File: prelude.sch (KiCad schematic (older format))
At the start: 34 parts, among them J1 CONN_01X50, J2 USB_C, J3 CONN_01X04, SW1 SW_Push, U1 LM3671MF-3.3, U2 STM32F103RETx, U3 AP5724, Y1 16MHz

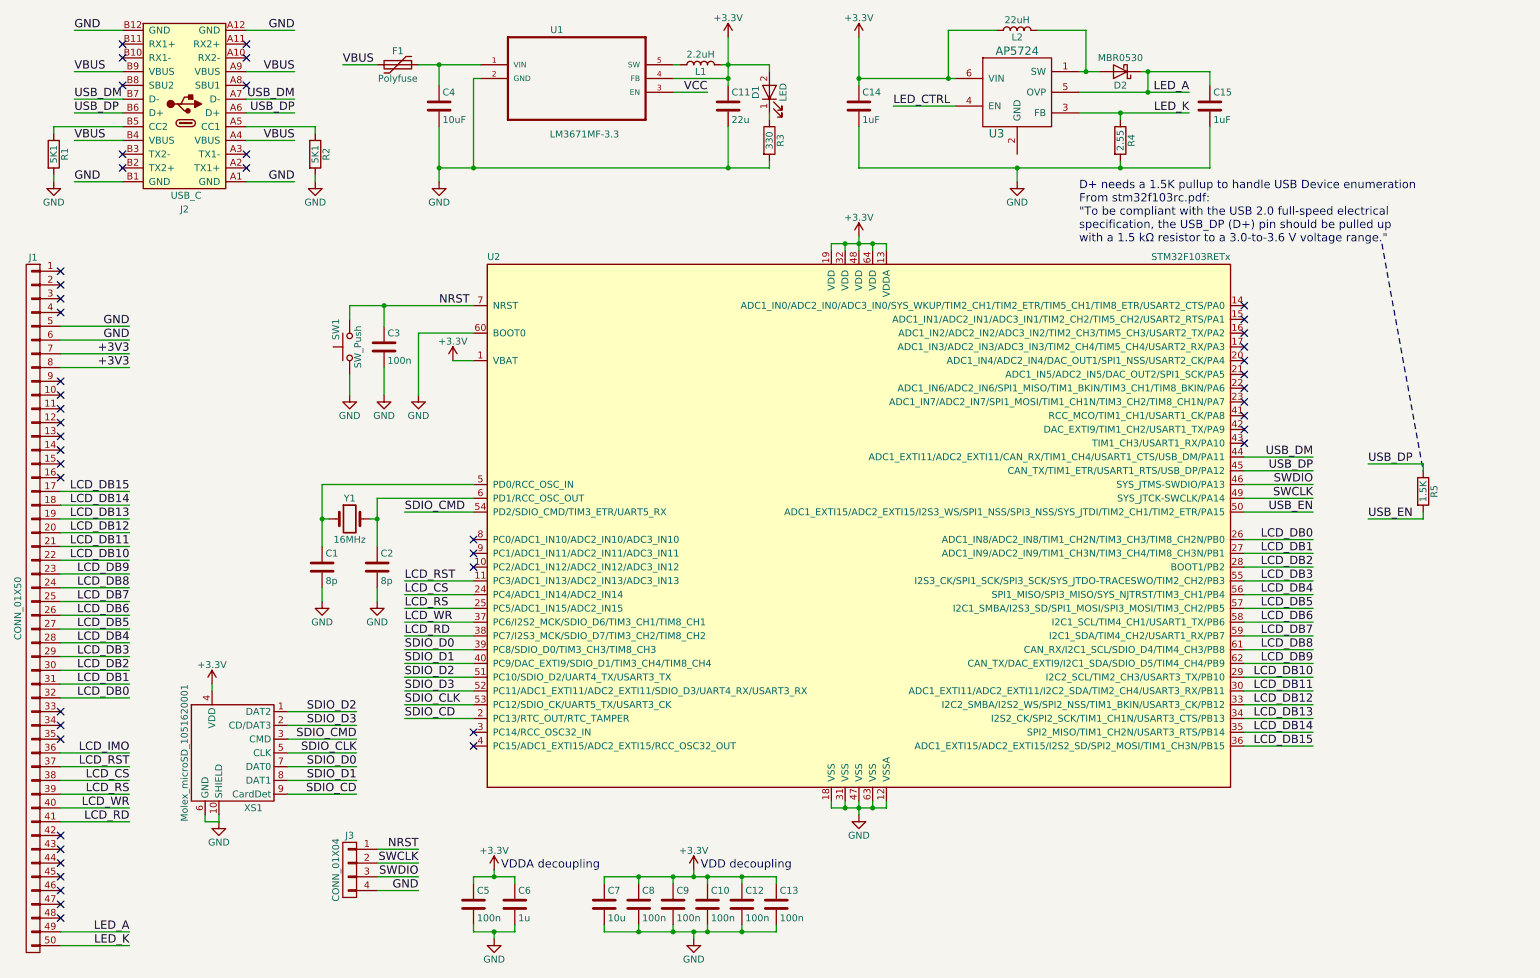
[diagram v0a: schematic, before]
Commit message: Moved to STM32F411RE
Had to move to different MCU (STM32F411RE) because I2C bus was fixed to pins on B bus, which was used for LCD data bus, and SDIO was also fixed to C bus.
Remapped LCD data bus to C bus since it allows having all other functionality (SDIO, I2C, USB) correctly mapped.
Redid CvPcb and net generation.
Started PCB routing with MCU pins 49-64 facing LCD connector.
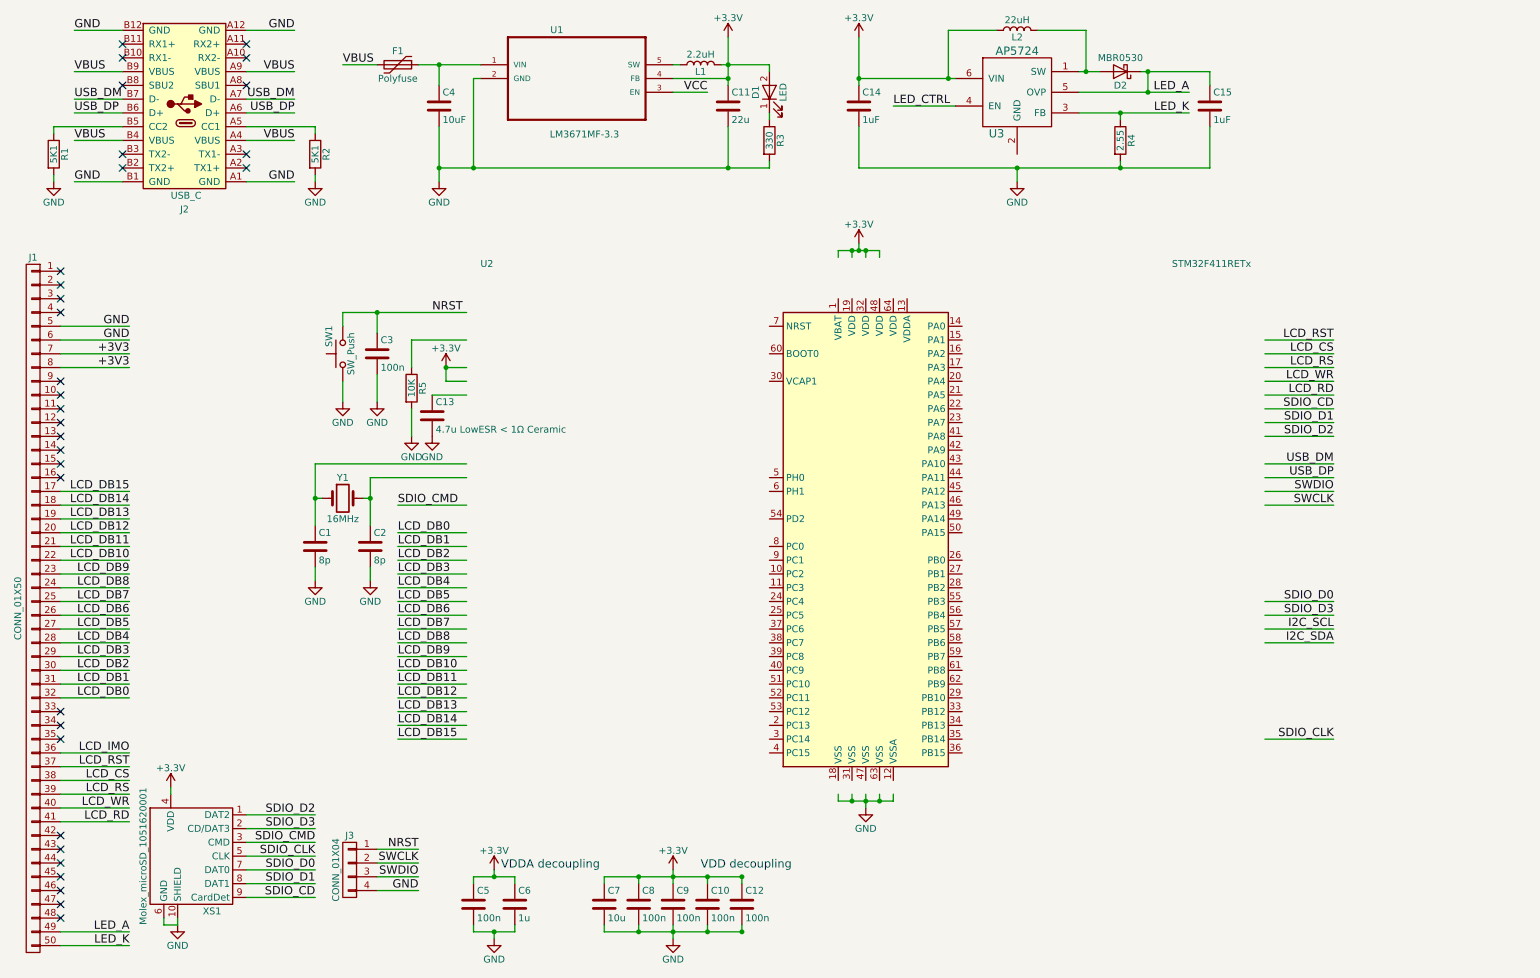
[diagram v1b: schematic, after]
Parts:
- removed U2: STM32F103RETx, Housings_QFP:LQFP-64_10x10mm_Pitch0.5mm, symbol STM32F103RETx
- added U2: STM32F411RETx, LQFP64, symbol STM32F411RETx
- C13: value 100n -> 4.7u LowESR < 1Ω Ceramic
- R5: value 1.5K -> 10K; footprint Resistors_SMD:R_0805 -> (none)
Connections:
- net labels added: I2C_SCL, I2C_SDA
- net labels removed: USB_EN
- wire segments 185 -> 217
- no-connect marks 48 -> 32
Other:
- note removed: "D+ needs a 1.5K pullup to handle USB Device enumeration\nFrom stm32f103rc.pdf:\n"To be compliant with the USB 2.0 full-speed electrical\nspecification, the USB_DP (D+) pin should be pulled up\nwith a 1.5 kΩ resistor to a 3.0-to-3.6 V voltage range.""
- moved on the sheet: C1, C2, C3, SW1, XS1, Y1

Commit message: A lot of changes, just need to add more polish and clean up
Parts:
- removed XS1: Molex_microSD_1051620001, volium:Molex_1051620001, symbol Molex_microSD_1051620001
- added J4: CONN_01X08, volium:WE_68710814022, symbol CONN_01X08
- added R6: 10K, Resistors_SMD:R_0805, symbol R
- added XS1: SD_ebay-uSD-push/push_SMD, volium:Conn_uSDcard, symbol SD_ebay-uSD-push/push_SMD
- J2: footprint volium:DX07S024XJ1 -> volium:Amphenol_12401548E4#2A
- J3: footprint Pin_Headers:Pin_Header_Angled_1x04_Pitch2.54mm -> volium:M20-8890445
- R5: footprint (none) -> Resistors_SMD:R_0805
- U2: footprint LQFP64 -> Housings_QFP:LQFP-64_10x10mm_Pitch0.5mm
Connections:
- net labels added: TS_INT, TS_RST, TS_SCL, TS_SDA, USB_D+, USB_D-
- net labels removed: I2C_SCL, I2C_SDA
- wire segments 217 -> 192
- no-connect marks 32 -> 33
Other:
- note added: "Pin 32"
- note added: "Pin 48"
- note added: "Pin 64"

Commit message: Updates project after loading with KiCad 5.0.2
Replaced schematic symbols and pcb footprints with new versions
Regenerated netlist after all changes
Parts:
- removed J3: CONN_01X04, volium:M20-8890445, symbol CONN_01X04
- removed J4: CONN_01X08, volium:WE_68710814022, symbol CONN_01X08
- removed SW1: SW_Push, Buttons_Switches_SMD:SW_SPST_PTS645, symbol SW_Push
- removed U2: STM32F411RETx, Housings_QFP:LQFP-64_10x10mm_Pitch0.5mm, symbol STM32F411RETx
- removed XS1: SD_ebay-uSD-push/push_SMD, volium:Conn_uSDcard, symbol SD_ebay-uSD-push/push_SMD
- added J3: Conn_01x04, volium:M20-8890445, symbol Connector_Generic:Conn_01x04
- added J4: Conn_01x08, volium:WE_68710814022, symbol Connector_Generic:Conn_01x08
- added SW1: SW_Push, Button_Switch_SMD:SW_SPST_PTS645, symbol Switch:SW_Push
- added U2: STM32F411RETx, Package_QFP:LQFP-64_10x10mm_P0.5mm, symbol MCU_ST_STM32F4:STM32F411RETx
- added XS1: SD_ebay-uSD-push_push_SMD, volium:Conn_uSDcard, symbol volium:SD_ebay-uSD-push_push_SMD
- C1, C10, C11, C12, C13, C14, C15, C2, C3, C4, C5, C6, C7, C8, C9: footprint Capacitors_SMD:C_0805 -> Capacitor_SMD:C_0805_2012Metric_Pad1.15x1.40mm_HandSolder; symbol C -> Device:C
- D1: footprint LEDs:LED_0805 -> LED_SMD:LED_0805_2012Metric_Pad1.15x1.40mm_HandSolder; symbol LED -> Device:LED
- D2: footprint Diodes_SMD:D_SOD-123 -> Diode_SMD:D_SOD-123; symbol D_Schottky -> Device:D_Schottky
- F1: symbol Polyfuse -> Device:Polyfuse
- J1: symbol CONN_01X50 -> volium:CONN_01X50
- J2: symbol USB_C -> volium:USB_C
- L1: footprint Inductors:Inductor_Taiyo-Yuden_NR-24xx -> Inductor_SMD:L_Taiyo-Yuden_NR-24xx_HandSoldering; symbol L -> Device:L
- L2: footprint Inductors:Inductor_Taiyo-Yuden_NR-30xx -> Inductor_SMD:L_Taiyo-Yuden_NR-30xx_HandSoldering; symbol L -> Device:L
- R1, R2, R3, R4, R5, R6: footprint Resistors_SMD:R_0805 -> Resistor_SMD:R_0805_2012Metric_Pad1.15x1.40mm_HandSolder; symbol R -> Device:R
- U1: footprint TO_SOT_Packages_SMD:TSOT-23-5 -> Package_TO_SOT_SMD:SOT-23-5_HandSoldering; symbol LM3671MF-3.3 -> volium:LM3671MF-3.3
- U3: footprint TO_SOT_Packages_SMD:SOT-23-6 -> Package_TO_SOT_SMD:SOT-23-6_Handsoldering; symbol AP5724 -> volium:AP5724
- Y1: footprint Crystals:Crystal_SMD_5032-2pin_5.0x3.2mm -> Crystal:Crystal_SMD_5032-2Pin_5.0x3.2mm_HandSoldering; symbol Crystal -> Device:Crystal
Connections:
- net labels removed: LCD_IMO, USB_DM, USB_DP
- wire segments 192 -> 231
- no-connect marks 33 -> 45
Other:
- moved on the sheet: C1, C13, C2, C3, R5, Y1

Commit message: Replaces passive components with regular (non-HandSolder) versions
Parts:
- C1, C10, C11, C12, C13, C14, C15, C2, C3, C4, C5, C6, C7, C8, C9: footprint Capacitor_SMD:C_0805_2012Metric_Pad1.15x1.40mm_HandSolder -> Capacitor_SMD:C_0805_2012Metric
- D1: footprint LED_SMD:LED_0805_2012Metric_Pad1.15x1.40mm_HandSolder -> LED_SMD:LED_0805_2012Metric
- L1: footprint Inductor_SMD:L_Taiyo-Yuden_NR-24xx_HandSoldering -> Inductor_SMD:L_Taiyo-Yuden_NR-24xx
- L2: footprint Inductor_SMD:L_Taiyo-Yuden_NR-30xx_HandSoldering -> Inductor_SMD:L_Taiyo-Yuden_NR-30xx
- R1, R2, R3, R4, R5, R6: footprint Resistor_SMD:R_0805_2012Metric_Pad1.15x1.40mm_HandSolder -> Resistor_SMD:R_0805_2012Metric
- Y1: footprint Crystal:Crystal_SMD_5032-2Pin_5.0x3.2mm_HandSoldering -> Crystal:Crystal_SMD_5032-2Pin_5.0x3.2mm
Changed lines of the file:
@@
 F 0 "L2" V 7850 750 50  0000 C CNN
 F 1 "22uH" V 7975 750 50  0000 C CNN
-F 2 "Inductor_SMD:L_Taiyo-Yuden_NR-30xx_HandSoldering" H 7900 750 50  0001 C CNN
+F 2 "Inductor_SMD:L_Taiyo-Yuden_NR-30xx" H 7900 750 50  0001 C CNN
 F 3 "" H 7900 750 50  0001 C CNN
 	1    7900 750
@@
 F 0 "C14" H 6775 1400 50  0000 L CNN
 F 1 "1uF" H 6775 1200 50  0000 L CNN
-F 2 "Capacitor_SMD:C_0805_2012Metric_Pad1.15x1.40mm_HandSolder" H 6788 1150 50  0001 C CNN
+F 2 "Capacitor_SMD:C_0805_2012Metric" H 6788 1150 50  0001 C CNN
 F 3 "" H 6750 1300 50  0001 C CNN
 	1    6750 1300
@@
 F 0 "C15" H 9325 1400 50  0000 L CNN
 F 1 "1uF" H 9325 1200 50  0000 L CNN
-F 2 "Capacitor_SMD:C_0805_2012Metric_Pad1.15x1.40mm_HandSolder" H 9338 1150 50  0001 C CNN
+F 2 "Capacitor_SMD:C_0805_2012Metric" H 9338 1150 50  0001 C CNN
 F 3 "" H 9300 1300 50  0001 C CNN
 	1    9300 1300
@@
 F 0 "R4" V 8730 1550 50  0000 C CNN
 F 1 "2.55" V 8650 1550 50  0000 C CNN
-F 2 "Resistor_SMD:R_0805_2012Metric_Pad1.15x1.40mm_HandSolder" V 8580 1550 50  0001 C CNN
+F 2 "Resistor_SMD:R_0805_2012Metric" V 8580 1550 50  0001 C CNN
 F 3 "" H 8650 1550 50  0001 C CNN
 	1    8650 1550
@@
 F 0 "C4" H 3725 1400 50  0000 L CNN
 F 1 "10uF" H 3725 1200 50  0000 L CNN
-F 2 "Capacitor_SMD:C_0805_2012Metric_Pad1.15x1.40mm_HandSolder" H 3738 1150 50  0001 C CNN
+F 2 "Capacitor_SMD:C_0805_2012Metric" H 3738 1150 50  0001 C CNN
 F 3 "" H 3700 1300 50  0001 C CNN
 	1    3700 1300
@@
 F 0 "C11" H 5825 1400 50  0000 L CNN
 F 1 "22u" H 5825 1200 50  0000 L CNN
-F 2 "Capacitor_SMD:C_0805_2012Metric_Pad1.15x1.40mm_HandSolder" H 5838 1150 50  0001 C CNN
+F 2 "Capacitor_SMD:C_0805_2012Metric" H 5838 1150 50  0001 C CNN
 F 3 "" H 5800 1300 50  0001 C CNN
 	1    5800 1300
@@
 F 0 "D1" H 6100 1300 50  0000 C CNN
 F 1 "LED" H 6100 1100 50  0000 C CNN
-F 2 "LED_SMD:LED_0805_2012Metric_Pad1.15x1.40mm_HandSolder" H 6100 1200 50  0001 C CNN
+F 2 "LED_SMD:LED_0805_2012Metric" H 6100 1200 50  0001 C CNN
 F 3 "" H 6100 1200 50  0001 C CNN
 	1    6100 1200
@@
 F 0 "R3" V 6180 1550 50  0000 C CNN
 F 1 "330" V 6100 1550 50  0000 C CNN
-F 2 "Resistor_SMD:R_0805_2012Metric_Pad1.15x1.40mm_HandSolder" V 6030 1550 50  0001 C CNN
+F 2 "Resistor_SMD:R_0805_2012Metric" V 6030 1550 50  0001 C CNN
 F 3 "" H 6100 1550 50  0001 C CNN
 	1    6100 1550
@@
 F 0 "L1" V 5550 1000 50  0000 C CNN
 F 1 "2.2uH" V 5675 1000 50  0000 C CNN
-F 2 "Inductor_SMD:L_Taiyo-Yuden_NR-24xx_HandSoldering" H 5600 1000 50  0001 C CNN
+F 2 "Inductor_SMD:L_Taiyo-Yuden_NR-24xx" H 5600 1000 50  0001 C CNN
 F 3 "" H 5600 1000 50  0001 C CNN
 	1    5600 1000
@@
 F 0 "R1" V 980 1650 50  0000 C CNN
 F 1 "5K1" V 900 1650 50  0000 C CNN
-F 2 "Resistor_SMD:R_0805_2012Metric_Pad1.15x1.40mm_HandSolder" V 830 1650 50  0001 C CNN
+F 2 "Resistor_SMD:R_0805_2012Metric" V 830 1650 50  0001 C CNN
 F 3 "" H 900 1650 50  0001 C CNN
 	1    900  1650
@@
 F 0 "R2" V 2880 1650 50  0000 C CNN
 F 1 "5K1" V 2800 1650 50  0000 C CNN
-F 2 "Resistor_SMD:R_0805_2012Metric_Pad1.15x1.40mm_HandSolder" V 2730 1650 50  0001 C CNN
+F 2 "Resistor_SMD:R_0805_2012Metric" V 2730 1650 50  0001 C CNN
 F 3 "" H 2800 1650 50  0001 C CNN
 	1    2800 1650
@@
 F 0 "C3" H 3975 3200 50  0000 L CNN
 F 1 "100n" H 3975 3000 50  0000 L CNN
-F 2 "Capacitor_SMD:C_0805_2012Metric_Pad1.15x1.40mm_HandSolder" H 3988 2950 50  0001 C CNN
+F 2 "Capacitor_SMD:C_0805_2012Metric" H 3988 2950 50  0001 C CNN
 F 3 "" H 3950 3100 50  0001 C CNN
 	1    3950 3100
@@
 F 0 "Y1" H 3700 4300 50  0000 C CNN
 F 1 "16MHz" H 3700 4000 50  0000 C CNN
-F 2 "Crystal:Crystal_SMD_5032-2Pin_5.0x3.2mm_HandSoldering" H 3700 4150 50  0001 C CNN
+F 2 "Crystal:Crystal_SMD_5032-2Pin_5.0x3.2mm" H 3700 4150 50  0001 C CNN
 F 3 "" H 3700 4150 50  0001 C CNN
 	1    3700 4150
@@
 F 0 "C1" H 3525 4600 50  0000 L CNN
 F 1 "8p" H 3525 4400 50  0000 L CNN
-F 2 "Capacitor_SMD:C_0805_2012Metric_Pad1.15x1.40mm_HandSolder" H 3538 4350 50  0001 C CNN
+F 2 "Capacitor_SMD:C_0805_2012Metric" H 3538 4350 50  0001 C CNN
 F 3 "" H 3500 4500 50  0001 C CNN
 	1    3500 4500
@@
 F 0 "C2" H 3925 4600 50  0000 L CNN
 F 1 "8p" H 3925 4400 50  0000 L CNN
-F 2 "Capacitor_SMD:C_0805_2012Metric_Pad1.15x1.40mm_HandSolder" H 3938 4350 50  0001 C CNN
+F 2 "Capacitor_SMD:C_0805_2012Metric" H 3938 4350 50  0001 C CNN
 F 3 "" H 3900 4500 50  0001 C CNN
 	1    3900 4500
@@
 F 0 "C5" H 3975 7200 50  0000 L CNN
 F 1 "100n" H 3975 7000 50  0000 L CNN
-F 2 "Capacitor_SMD:C_0805_2012Metric_Pad1.15x1.40mm_HandSolder" H 3988 6950 50  0001 C CNN
+F 2 "Capacitor_SMD:C_0805_2012Metric" H 3988 6950 50  0001 C CNN
 F 3 "" H 3950 7100 50  0001 C CNN
 	1    3950 7100
@@
 F 0 "C6" H 4275 7200 50  0000 L CNN
 F 1 "1u" H 4275 7000 50  0000 L CNN
-F 2 "Capacitor_SMD:C_0805_2012Metric_Pad1.15x1.40mm_HandSolder" H 4288 6950 50  0001 C CNN
+F 2 "Capacitor_SMD:C_0805_2012Metric" H 4288 6950 50  0001 C CNN
 F 3 "" H 4250 7100 50  0001 C CNN
 	1    4250 7100
@@
 F 0 "C7" H 4925 7200 50  0000 L CNN
 F 1 "10u" H 4925 7000 50  0000 L CNN
-F 2 "Capacitor_SMD:C_0805_2012Metric_Pad1.15x1.40mm_HandSolder" H 4938 6950 50  0001 C CNN
+F 2 "Capacitor_SMD:C_0805_2012Metric" H 4938 6950 50  0001 C CNN
 F 3 "" H 4900 7100 50  0001 C CNN
 	1    4900 7100
@@
 F 0 "C8" H 5175 7200 50  0000 L CNN
 F 1 "100n" H 5175 7000 50  0000 L CNN
-F 2 "Capacitor_SMD:C_0805_2012Metric_Pad1.15x1.40mm_HandSolder" H 5188 6950 50  0001 C CNN
+F 2 "Capacitor_SMD:C_0805_2012Metric" H 5188 6950 50  0001 C CNN
 F 3 "" H 5150 7100 50  0001 C CNN
 	1    5150 7100
@@
 F 0 "C9" H 5425 7200 50  0000 L CNN
 F 1 "100n" H 5425 7000 50  0000 L CNN
-F 2 "Capacitor_SMD:C_0805_2012Metric_Pad1.15x1.40mm_HandSolder" H 5438 6950 50  0001 C CNN
+F 2 "Capacitor_SMD:C_0805_2012Metric" H 5438 6950 50  0001 C CNN
 F 3 "" H 5400 7100 50  0001 C CNN
 	1    5400 7100
@@
 F 0 "C10" H 5675 7200 50  0000 L CNN
 F 1 "100n" H 5675 7000 50  0000 L CNN
-F 2 "Capacitor_SMD:C_0805_2012Metric_Pad1.15x1.40mm_HandSolder" H 5688 6950 50  0001 C CNN
+F 2 "Capacitor_SMD:C_0805_2012Metric" H 5688 6950 50  0001 C CNN
 F 3 "" H 5650 7100 50  0001 C CNN
 	1    5650 7100
@@
 F 0 "C12" H 5925 7200 50  0000 L CNN
 F 1 "100n" H 5925 7000 50  0000 L CNN
-F 2 "Capacitor_SMD:C_0805_2012Metric_Pad1.15x1.40mm_HandSolder" H 5938 6950 50  0001 C CNN
+F 2 "Capacitor_SMD:C_0805_2012Metric" H 5938 6950 50  0001 C CNN
 F 3 "" H 5900 7100 50  0001 C CNN
 	1    5900 7100
@@
 F 0 "C13" H 4475 3650 50  0000 L CNN
 F 1 "4.7u  LowESR < 1Ω Ceramic" H 3100 3350 50  0000 L CNN
-F 2 "Capacitor_SMD:C_0805_2012Metric_Pad1.15x1.40mm_HandSolder" H 4488 3400 50  0001 C CNN
+F 2 "Capacitor_SMD:C_0805_2012Metric" H 4488 3400 50  0001 C CNN
 F 3 "" H 4450 3550 50  0001 C CNN
 	1    4450 3550
@@
 F 0 "R5" V 4280 3350 50  0000 C CNN
 F 1 "10K" V 4200 3350 50  0000 C CNN
-F 2 "Resistor_SMD:R_0805_2012Metric_Pad1.15x1.40mm_HandSolder" V 4130 3350 50  0001 C CNN
+F 2 "Resistor_SMD:R_0805_2012Metric" V 4130 3350 50  0001 C CNN
 F 3 "" H 4200 3350 50  0001 C CNN
 	1    4200 3350
@@
 F 0 "R6" V 7480 1550 50  0000 C CNN
 F 1 "10K" V 7400 1550 50  0000 C CNN
-F 2 "Resistor_SMD:R_0805_2012Metric_Pad1.15x1.40mm_HandSolder" V 7330 1550 50  0001 C CNN
+F 2 "Resistor_SMD:R_0805_2012Metric" V 7330 1550 50  0001 C CNN
 F 3 "" H 7400 1550 50  0001 C CNN
 	1    7400 1550

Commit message: Replaces J2 Connector (USB-C) with new D0-9062-005LG (SMD 16 terminals)
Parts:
- J2: footprint volium:Amphenol_12401548E4#2A -> volium:D0-9062-005LG
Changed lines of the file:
@@
 F 0 "J2" H 1850 2050 50  0000 C CNN
 F 1 "USB_C" H 1750 1950 50  0000 L CNN
-F 2 "volium:Amphenol_12401548E4#2A" H 2000 1450 50  0001 C CNN
+F 2 "volium:D0-9062-005LG" H 2000 1450 50  0001 C CNN
 F 3 "" H 2000 1450 50  0001 C CNN
 	1    1850 1300

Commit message: Minor update to schematic to include "F" in all values of capacitors
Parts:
- C1, C2: value 8p -> 8pF
- C10, C12, C3, C5, C8, C9: value 100n -> 100nF
- C11: value 22u -> 22uF
- C13: value 4.7u LowESR < 1Ω Ceramic -> 4.7uF LowESR < 1Ω Ceramic
- C6: value 1u -> 1uF
- C7: value 10u -> 10uF
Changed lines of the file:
@@
 EESchema Schematic File Version 4
 LIBS:prelude-cache
-EELAYER 26 0
+EELAYER 29 0
 EELAYER END
 $Descr A4 11693 8268
@@
 P 6750 1300
 F 0 "C14" H 6775 1400 50  0000 L CNN
-F 1 "1uF" H 6775 1200 50  0000 L CNN
+F 1 "1uF" H 6775 1200 45  0000 L CNN
 F 2 "Capacitor_SMD:C_0805_2012Metric" H 6788 1150 50  0001 C CNN
 F 3 "" H 6750 1300 50  0001 C CNN
@@
 P 9300 1300
 F 0 "C15" H 9325 1400 50  0000 L CNN
-F 1 "1uF" H 9325 1200 50  0000 L CNN
+F 1 "1uF" H 9325 1200 45  0000 L CNN
 F 2 "Capacitor_SMD:C_0805_2012Metric" H 9338 1150 50  0001 C CNN
 F 3 "" H 9300 1300 50  0001 C CNN
@@
 P 3700 1300
 F 0 "C4" H 3725 1400 50  0000 L CNN
-F 1 "10uF" H 3725 1200 50  0000 L CNN
+F 1 "10uF" H 3725 1200 45  0000 L CNN
 F 2 "Capacitor_SMD:C_0805_2012Metric" H 3738 1150 50  0001 C CNN
 F 3 "" H 3700 1300 50  0001 C CNN
@@
 P 5800 1300
 F 0 "C11" H 5825 1400 50  0000 L CNN
-F 1 "22u" H 5825 1200 50  0000 L CNN
+F 1 "22uF" H 5825 1200 45  0000 L CNN
 F 2 "Capacitor_SMD:C_0805_2012Metric" H 5838 1150 50  0001 C CNN
 F 3 "" H 5800 1300 50  0001 C CNN
@@
 P 3950 3100
 F 0 "C3" H 3975 3200 50  0000 L CNN
-F 1 "100n" H 3975 3000 50  0000 L CNN
+F 1 "100nF" H 3975 3000 45  0000 L CNN
 F 2 "Capacitor_SMD:C_0805_2012Metric" H 3988 2950 50  0001 C CNN
 F 3 "" H 3950 3100 50  0001 C CNN
@@
 P 3500 4500
 F 0 "C1" H 3525 4600 50  0000 L CNN
-F 1 "8p" H 3525 4400 50  0000 L CNN
+F 1 "8pF" H 3525 4400 45  0000 L CNN
 F 2 "Capacitor_SMD:C_0805_2012Metric" H 3538 4350 50  0001 C CNN
 F 3 "" H 3500 4500 50  0001 C CNN
@@
 P 3900 4500
 F 0 "C2" H 3925 4600 50  0000 L CNN
-F 1 "8p" H 3925 4400 50  0000 L CNN
+F 1 "8pF" H 3925 4400 45  0000 L CNN
 F 2 "Capacitor_SMD:C_0805_2012Metric" H 3938 4350 50  0001 C CNN
 F 3 "" H 3900 4500 50  0001 C CNN
@@
 P 3950 7100
 F 0 "C5" H 3975 7200 50  0000 L CNN
-F 1 "100n" H 3975 7000 50  0000 L CNN
+F 1 "100nF" H 3975 7000 45  0000 L CNN
 F 2 "Capacitor_SMD:C_0805_2012Metric" H 3988 6950 50  0001 C CNN
 F 3 "" H 3950 7100 50  0001 C CNN
@@
 P 4250 7100
 F 0 "C6" H 4275 7200 50  0000 L CNN
-F 1 "1u" H 4275 7000 50  0000 L CNN
+F 1 "1uF" H 4275 7000 45  0000 L CNN
 F 2 "Capacitor_SMD:C_0805_2012Metric" H 4288 6950 50  0001 C CNN
 F 3 "" H 4250 7100 50  0001 C CNN
@@
 P 4900 7100
 F 0 "C7" H 4925 7200 50  0000 L CNN
-F 1 "10u" H 4925 7000 50  0000 L CNN
+F 1 "10uF" H 4925 7000 45  0000 L CNN
 F 2 "Capacitor_SMD:C_0805_2012Metric" H 4938 6950 50  0001 C CNN
 F 3 "" H 4900 7100 50  0001 C CNN
@@
 P 5150 7100
 F 0 "C8" H 5175 7200 50  0000 L CNN
-F 1 "100n" H 5175 7000 50  0000 L CNN
+F 1 "100nF" H 5175 7000 45  0000 L CNN
 F 2 "Capacitor_SMD:C_0805_2012Metric" H 5188 6950 50  0001 C CNN
 F 3 "" H 5150 7100 50  0001 C CNN
@@
 P 5400 7100
 F 0 "C9" H 5425 7200 50  0000 L CNN
-F 1 "100n" H 5425 7000 50  0000 L CNN
+F 1 "100nF" H 5425 7000 45  0000 L CNN
 F 2 "Capacitor_SMD:C_0805_2012Metric" H 5438 6950 50  0001 C CNN
 F 3 "" H 5400 7100 50  0001 C CNN
@@
 P 5650 7100
 F 0 "C10" H 5675 7200 50  0000 L CNN
-F 1 "100n" H 5675 7000 50  0000 L CNN
+F 1 "100nF" H 5675 7000 45  0000 L CNN
 F 2 "Capacitor_SMD:C_0805_2012Metric" H 5688 6950 50  0001 C CNN
 F 3 "" H 5650 7100 50  0001 C CNN
@@
 P 5900 7100
 F 0 "C12" H 5925 7200 50  0000 L CNN
-F 1 "100n" H 5925 7000 50  0000 L CNN
+F 1 "100nF" H 5925 7000 45  0000 L CNN
 F 2 "Capacitor_SMD:C_0805_2012Metric" H 5938 6950 50  0001 C CNN
 F 3 "" H 5900 7100 50  0001 C CNN
@@
 P 4450 3550
 F 0 "C13" H 4475 3650 50  0000 L CNN
-F 1 "4.7u  LowESR < 1Ω Ceramic" H 3100 3350 50  0000 L CNN
+F 1 "4.7uF  LowESR < 1Ω Ceramic" H 3100 3350 45  0000 L CNN
 F 2 "Capacitor_SMD:C_0805_2012Metric" H 4488 3400 50  0001 C CNN
 F 3 "" H 4450 3550 50  0001 C CNN
